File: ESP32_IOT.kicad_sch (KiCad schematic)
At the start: 0 parts

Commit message: Libraries and 1st page schem
Include the libraries of components and footprints and the 1st page of the schematic
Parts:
- added C1, C2, C5: 0.1, symbol Device:C
- added C2: 1, symbol Device:C
- added C3, C4: 10, symbol Device:C_Polarized
- added F1: 0ZCH0110AF2E, Footprints:FUSC3226X100N, symbol 0ZCH0110AF2E:0ZCH0110AF2E
- added J1: SS-52400-002, SS-52400-002:BELFUSE_SS-52400-002, symbol SS-52400-002:SS-52400-002
- added J2: B2B-PH-SM4-TB, B2B-PH-SM4-TB:JST_B2B-PH-SM4-TB, symbol B2B-PH-SM4-TB:B2B-PH-SM4-TB
- added LED1, LED4: LTST-C170KRKT, LEDC2012X120N, symbol LTST-C170KRKT:LTST-C170KRKT
- added LED2: LTST-C170GKT, LEDC2012X120N, symbol LTST-C170GKT:LTST-C170GKT
- added LED3: LTST-C170TBKT, LEDC2012X120N, symbol LTST-C170TBKT:LTST-C170TBKT
- added R1, R2: 10K, symbol Device:R
- added R10, R7, R8, R9: 470, symbol Device:R
- added R3, R4: 5K1, symbol Device:R
- added R5: 2K, symbol Device:R
- added R6: 20K, symbol Device:R
- added U1: MCP73871, Package_DFN_QFN:QFN-20-1EP_4x4mm_P0.5mm_EP2.5x2.5mm, symbol Battery_Management:MCP73871
- added VR1: LM1117MPX-3.3, LM1117MPX-3.3:VREG_LM1117MPX-3.3, symbol LM1117MPX-3.3:LM1117MPX-3.3
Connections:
- new net: C1.1, F1.1, J1.B4 (VBUSB1)
- new net: J1.B5 (CC2), R3.1
- new net: R2.2, U1.5 (THERM)
- new net: R1.2, U1.9 (~{TE})
- new net: R8.1, U1.8 (STAT1/~{LBO})
- new net: LED2.1 (K), R8.2
- new net: LED3.1 (K), R9.2
- new net: R5.2, U1.13 (PROG1)
- new net: LED1.1 (K), R7.2
- new net: J1.A5 (CC1), R4.1
- new net: R7.1, U1.7 (STAT2)
- new net: R6.2, U1.12 (PROG3)
- new net: R9.1, U1.6 (~{PG})
- new net +3V3: C4.1, C5.1, LED4.2 (A), VR1.2 (VOUT_2), VR1.4 (VOUT_4)
- new net +5V: C2.1, C3.1, U1.1 (OUT), U1.20 (OUT), VR1.3 (VIN)
- new net +5V_USB: C2.1, F1.2, LED1.2 (A), LED2.2 (A), LED3.2 (A), U1.17 (CE), U1.18 (IN), U1.19 (IN), U1.2 (VPCC)
- new net GND: C1.2, C2.2, C2.2, C3.2, C4.2, C5.2, J1.A1 (GNDA1), J1.A12 (GNDA2), J1.B1 (GNDB1), J1.B12 (GNDB2), J1.G1 (GND/SHIELD), J1.G2 (GND/SHIELD), J1.G3 (GND/SHIELD), J1.G4 (GND/SHIELD), J1.S1 (GND/SHIELD), J1.S2 (GND/SHIELD), J1.S3 (GND/SHIELD), J1.S4 (GND/SHIELD), J2.1, R1.1, R10.1, R2.1, R3.2, R4.2, R5.1, R6.1, U1.10 (V_{SS}), U1.11 (V_{SS}), U1.21 (V_{SS}), VR1.1 (GND)
- new net PWR_LED: LED4.1 (K), R10.2
- new net USB_DN: J1.A7 (DN1), J1.B7 (DN2)
- new net USB_DP: J1.A6 (DP1), J1.B6 (DP2)
- new net VBAT: J2.2, U1.14 (V_{BAT}), U1.15 (V_{BAT}), U1.16 (V_{BAT_SENSE})
- new net VBUS: J1.A4 (VBUSA1), J1.A9 (VBUSA2), J1.B9 (VBUSB2)
- no-connect marks 0 -> 10
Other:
- note added: "Battery JST Connector"
- note added: "LDO Voltage Regulator"
- note added: "LIPO Batery Charger"
- note added: "Power LED Indicator"
- note added: "USB-C Connector"

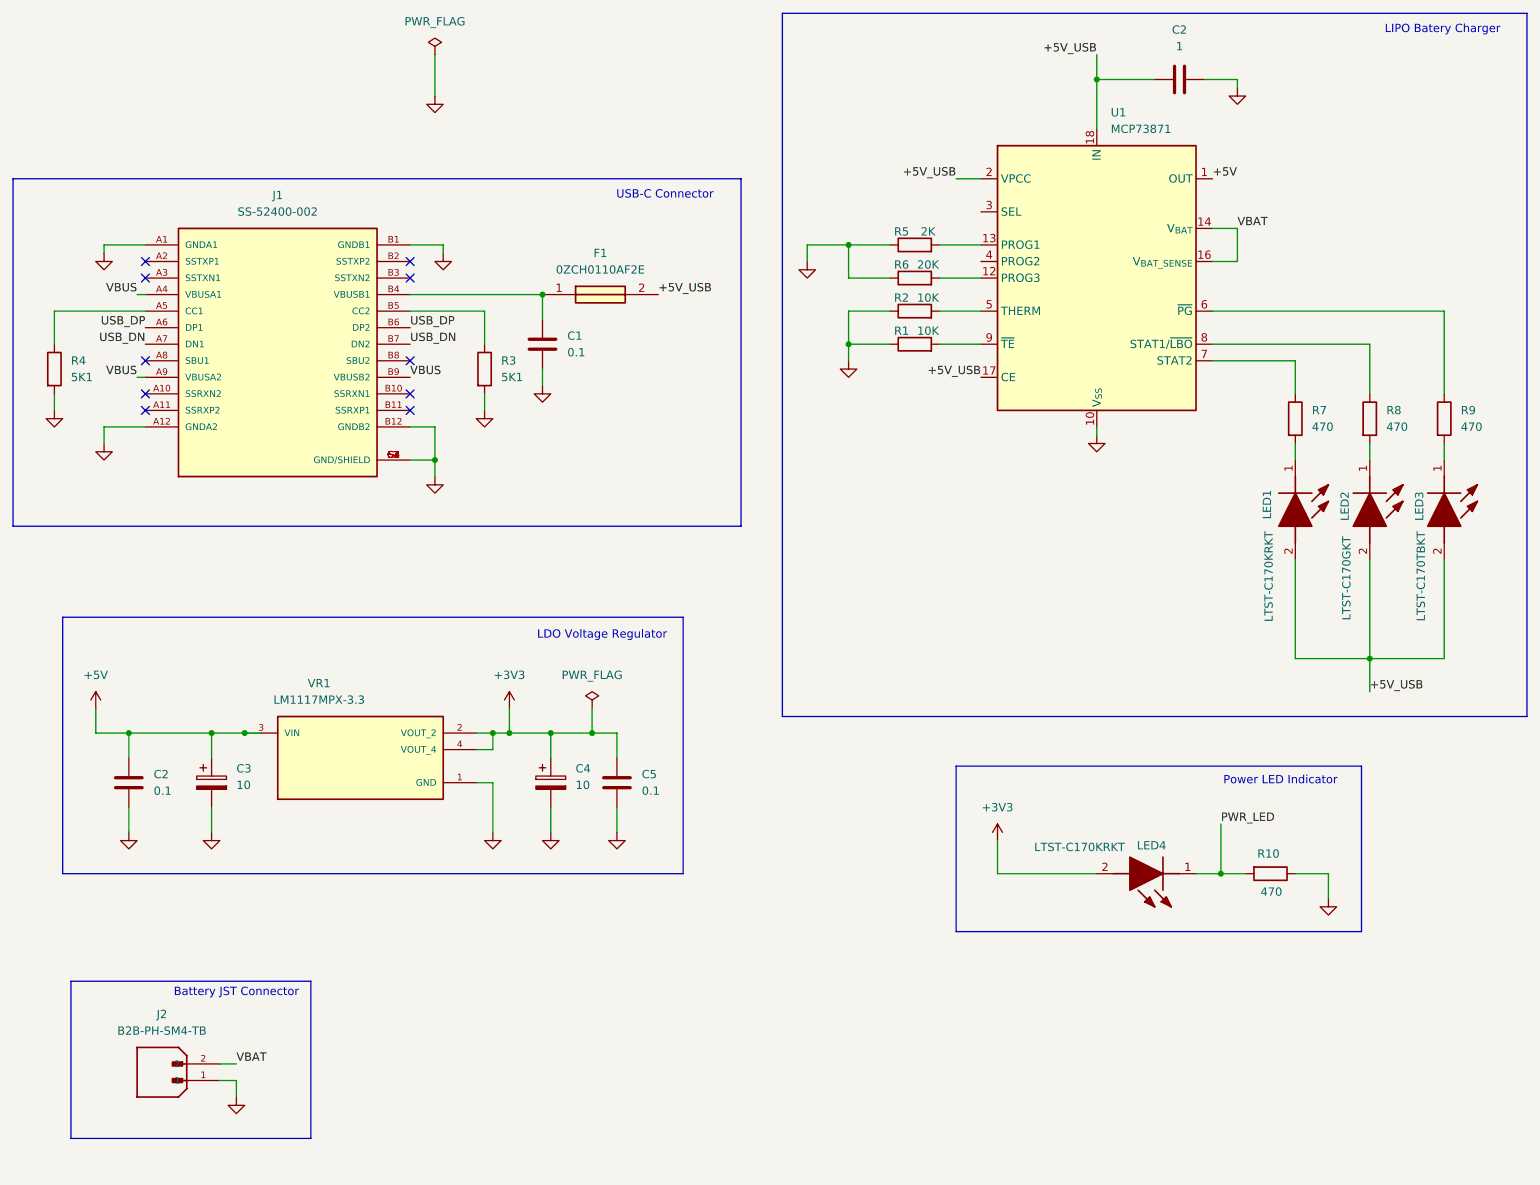
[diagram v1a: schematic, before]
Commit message: New page for ESP32
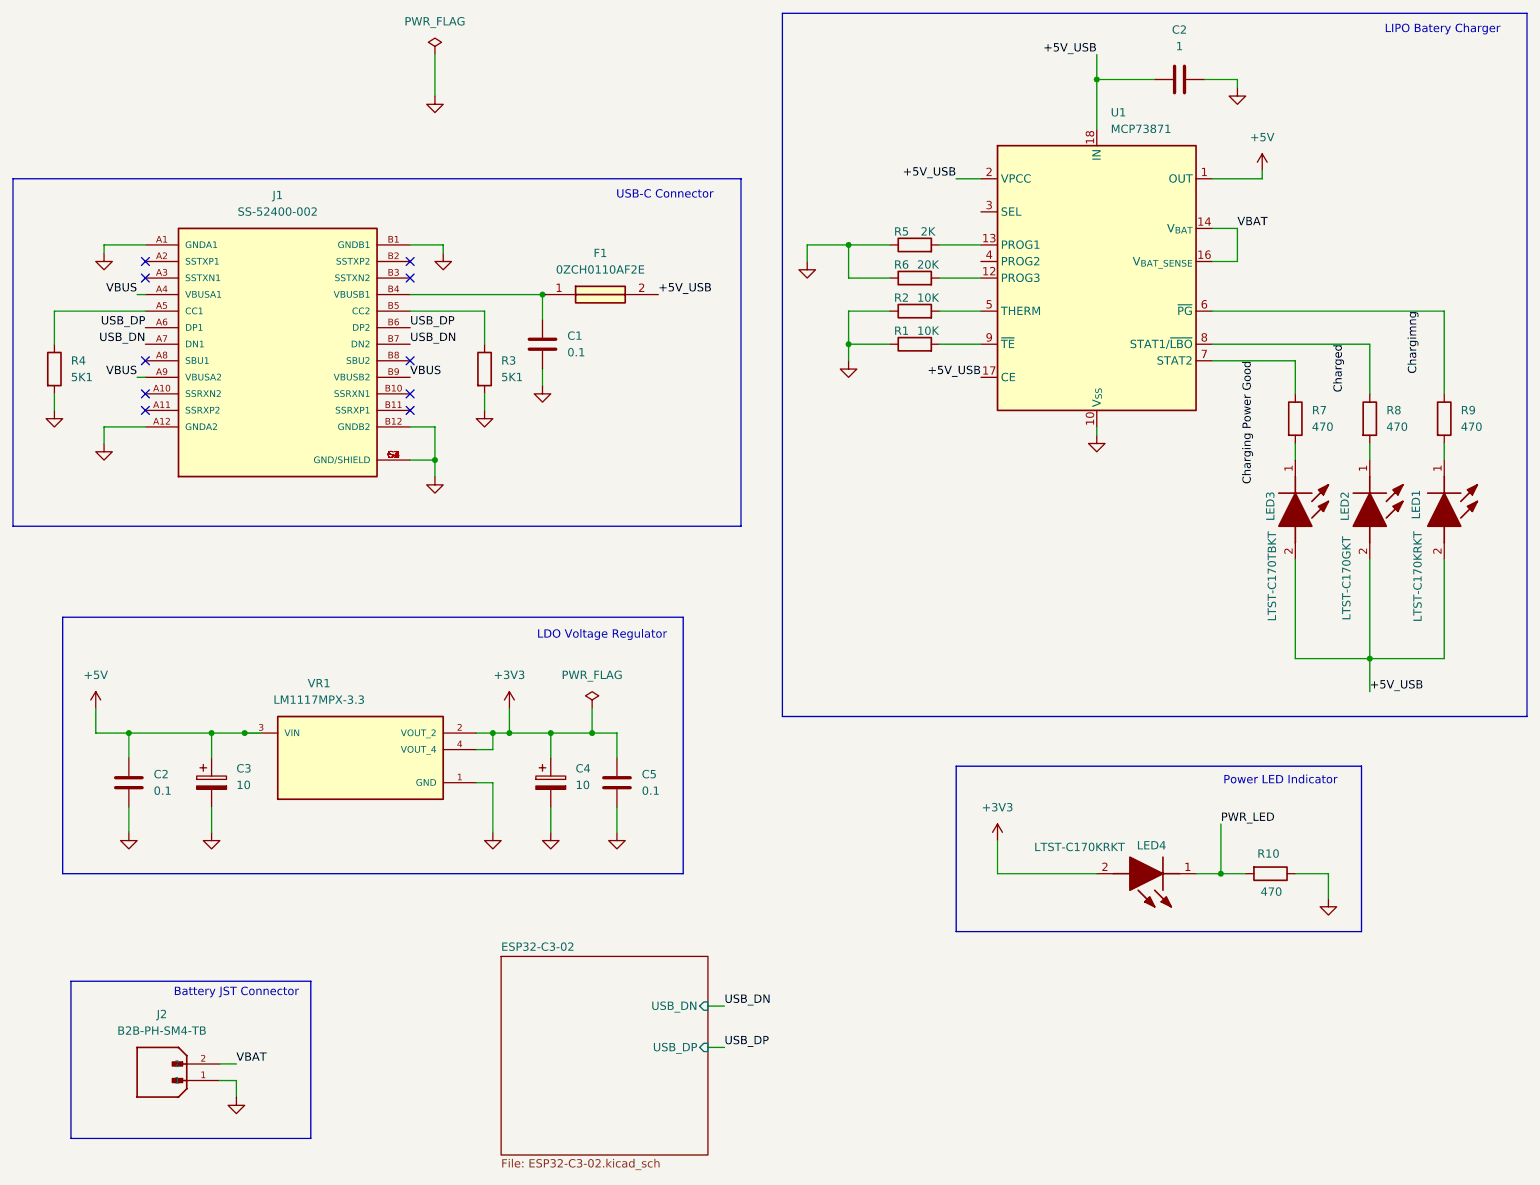
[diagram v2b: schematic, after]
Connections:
- net Charged: now reaches R8.1, U1.8 (STAT1/~{LBO})
- net at LED3.1 (K): now also R7.2; no longer R9.2
- net at LED1.1 (K): now also R9.2; no longer R7.2
- net Charging Power Good: now reaches R7.1, U1.7 (STAT2)
- net Chargimng: now reaches R9.1, U1.6 (~{PG})
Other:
- added sheet ESP32-C3-02 (ESP32-C3-02.kicad_sch)
- moved on the sheet: LED1, LED3

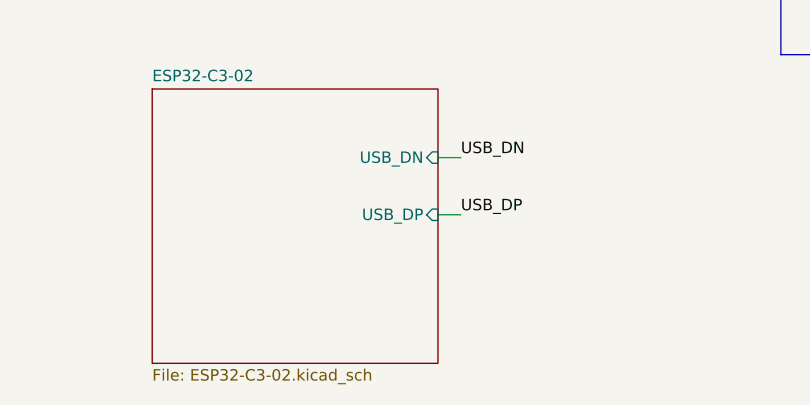
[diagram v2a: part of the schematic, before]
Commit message: More of the Page of ESP32
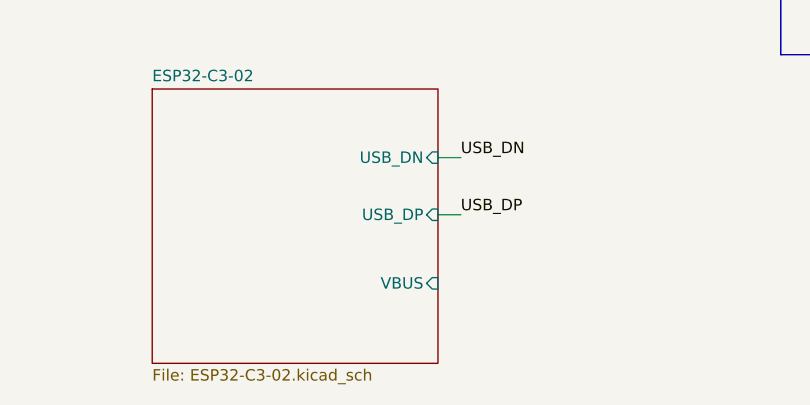
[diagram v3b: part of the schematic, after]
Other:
- sheet ESP32-C3-02 ports: added VBUS; removed none
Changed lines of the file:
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@@
+			)
+		)
+		(pin "VBUS" input
+			(at 132.08 187.96 0)
+			(effects
+				(font
+					(size 1.27 1.27)
+				)
+				(justify right)
 			)
 		)
